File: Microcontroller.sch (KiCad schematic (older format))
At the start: 22 parts, among them J3 Conn_02x03_Counter_Clockwise, U3 STM32F446VET6-sternie, U4 OSCILLATOR-sternie

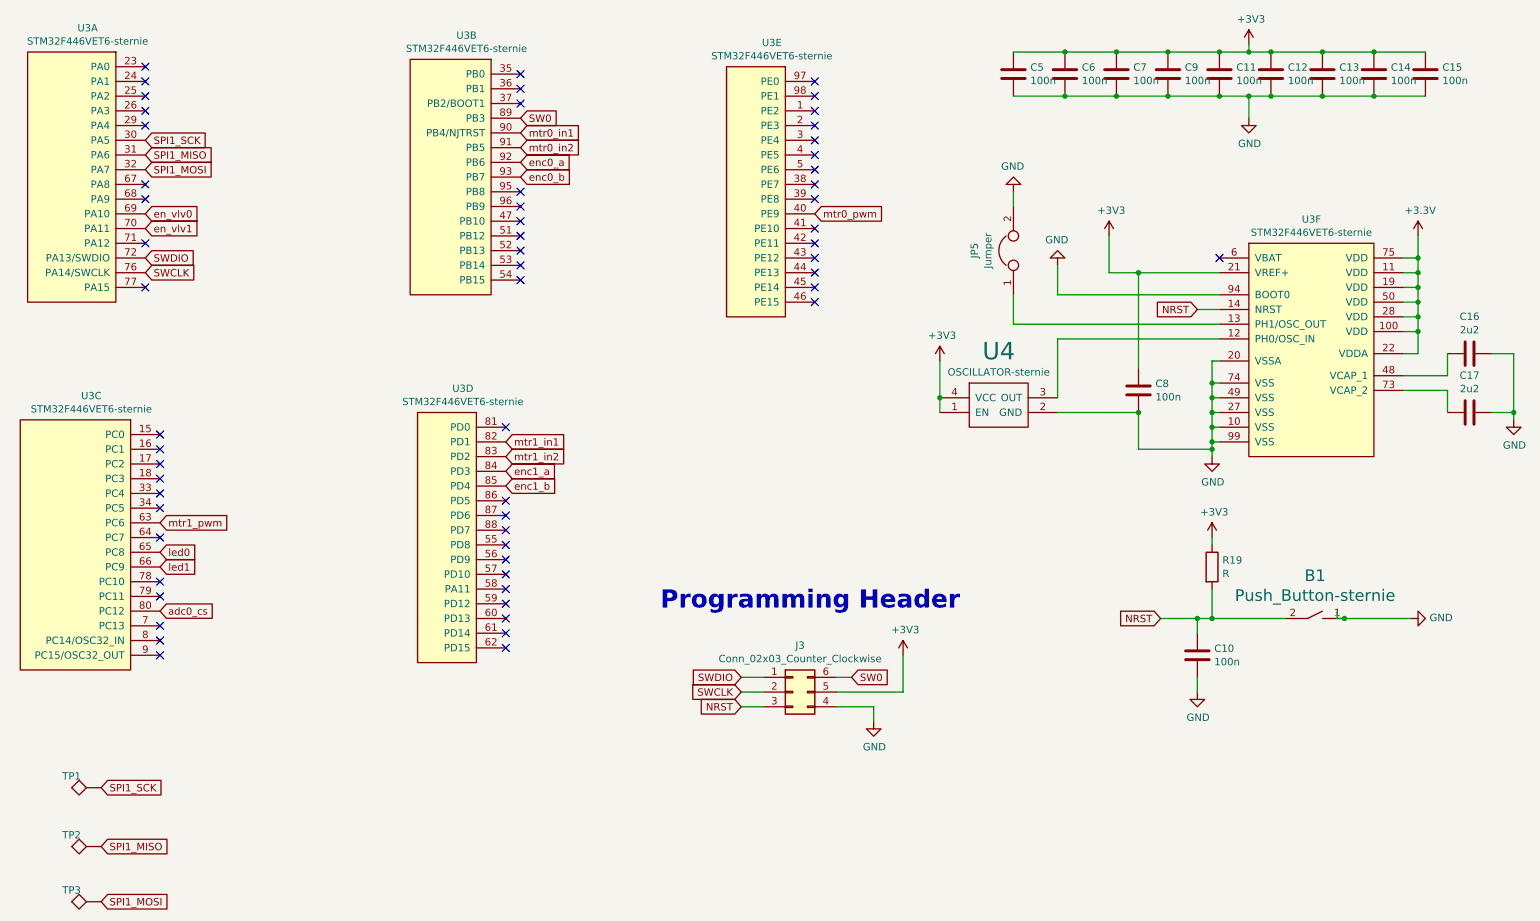
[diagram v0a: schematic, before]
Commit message: Formatting Changes
Made some minor formatting changes. Documented motor channels. Fixed in labels of motor channel.
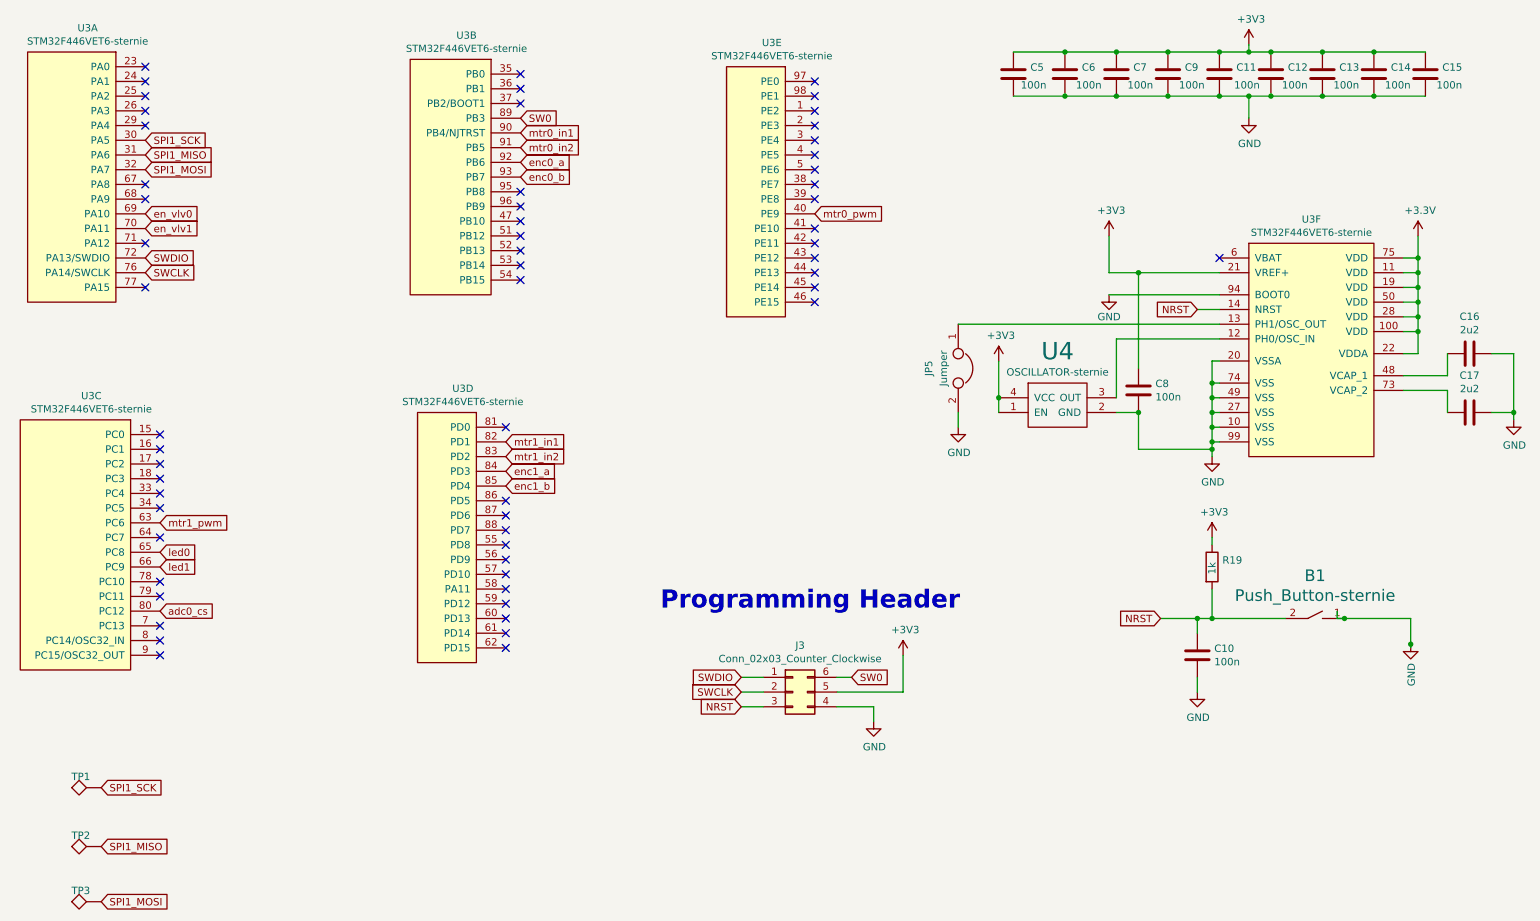
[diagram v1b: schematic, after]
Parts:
- R19: value R -> 1k
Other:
- moved on the sheet: JP5, U4
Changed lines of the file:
@@
 $Descr A4 11693 8268
 encoding utf-8
-Sheet 7 12
+Sheet 4 12
 Title ""
 Date ""
@@
 L bangbang_rev1-rescue:OSCILLATOR-sternie-engine_controller_series3-rescue U4
 U 1 1 5E54009F
-P 7550 3600
-F 0 "U4" H 7550 3966 118 0000 C CNN
-F 1 "OSCILLATOR-sternie" H 7550 3824 50  0000 C CNN
-F 2 "" H 7550 3600 118 0001 C CNN
-F 3 "" H 7550 3600 118 0001 C CNN
-	1    7550 3600
+P 7950 3600
+F 0 "U4" H 7950 3966 118 0000 C CNN
+F 1 "OSCILLATOR-sternie" H 7950 3824 50  0000 C CNN
+F 2 "" H 7950 3600 118 0001 C CNN
+F 3 "" H 7950 3600 118 0001 C CNN
+	1    7950 3600
 	1    0    0    -1
 $EndComp
@@
 	8900 2950 9050 2950
 Wire Wire Line
-	7950 3650 8500 3650
-Connection ~ 8500 3650
-Wire Wire Line
-	7150 3650 7150 3550
-Connection ~ 7150 3550
-Wire Wire Line
-	7150 3550 7150 3300
+	7550 3650 7550 3550
+Connection ~ 7550 3550
+Wire Wire Line
+	7550 3550 7550 3300
 $Comp
 L power:+3V3 #PWR036
 U 1 1 5E5FF2C5
-P 7150 3300
-F 0 "#PWR036" H 7150 3150 50  0001 C CNN
-F 1 "+3V3" H 7165 3473 50  0000 C CNN
-F 2 "" H 7150 3300 50  0001 C CNN
-F 3 "" H 7150 3300 50  0001 C CNN
-	1    7150 3300
-	1    0    0    -1
-$EndComp
-Wire Wire Line
-	7950 2650 7950 2850
-Wire Wire Line
-	7950 2850 9050 2850
+P 7550 3300
+F 0 "#PWR036" H 7550 3150 50  0001 C CNN
+F 1 "+3V3" H 7565 3473 50  0000 C CNN
+F 2 "" H 7550 3300 50  0001 C CNN
+F 3 "" H 7550 3300 50  0001 C CNN
+	1    7550 3300
+	1    0    0    -1
+$EndComp
 $Comp
 L power:+3V3 #PWR039
@@
 $EndComp
 $Comp
-L power:GND #PWR038
-U 1 1 5E604DB8
-P 7950 2650
-F 0 "#PWR038" H 7950 2400 50  0001 C CNN
-F 1 "GND" H 7955 2477 50  0000 C CNN
-F 2 "" H 7950 2650 50  0001 C CNN
-F 3 "" H 7950 2650 50  0001 C CNN
-	1    7950 2650
-	-1   0    0    1
-$EndComp
-Wire Wire Line
-	7950 3550 7950 3150
-Wire Wire Line
-	7950 3150 9050 3150
-Wire Wire Line
-	9050 3050 7650 3050
-Wire Wire Line
-	7650 3050 7650 2850
-$Comp
 L Device:Jumper JP5
 U 1 1 5E60F8B9
-P 7650 2550
-F 0 "JP5" H 7650 2814 50  0000 C CNN
-F 1 "Jumper" H 7650 2723 50  0000 C CNN
-F 2 "" H 7650 2550 50  0001 C CNN
-F 3 "~" H 7650 2550 50  0001 C CNN
-	1    7650 2550
-	0    -1   -1   0
-$EndComp
-Wire Wire Line
-	7650 2250 7650 2150
+P 7275 3350
+F 0 "JP5" H 7275 3150 50  0000 C CNN
+F 1 "Jumper" H 7275 3250 50  0000 C CNN
+F 2 "" H 7275 3350 50  0001 C CNN
+F 3 "~" H 7275 3350 50  0001 C CNN
+	1    7275 3350
+	0    1    1    0
+$EndComp
+Wire Wire Line
+	7275 3650 7275 3750
 $Comp
 L power:GND #PWR037
 U 1 1 5E6156CF
-P 7650 2150
-F 0 "#PWR037" H 7650 1900 50  0001 C CNN
-F 1 "GND" H 7655 1977 50  0000 C CNN
-F 2 "" H 7650 2150 50  0001 C CNN
-F 3 "" H 7650 2150 50  0001 C CNN
-	1    7650 2150
-	-1   0    0    1
+P 7275 3750
+F 0 "#PWR037" H 7275 3500 50  0001 C CNN
+F 1 "GND" H 7280 3577 50  0000 C CNN
+F 2 "" H 7275 3750 50  0001 C CNN
+F 3 "" H 7275 3750 50  0001 C CNN
+	1    7275 3750
+	1    0    0    -1
 $EndComp
 $Comp
@@
 P 8000 1350
 F 0 "C6" H 8115 1396 50  0000 L CNN
-F 1 "100n" H 8115 1305 50  0000 L CNN
+F 1 "100n" H 8075 1275 50  0000 L CNN
 F 2 "" H 8038 1200 50  0001 C CNN
 F 3 "~" H 8000 1350 50  0001 C CNN
@@
 P 8350 1350
 F 0 "C7" H 8465 1396 50  0000 L CNN
-F 1 "100n" H 8465 1305 50  0000 L CNN
+F 1 "100n" H 8425 1275 50  0000 L CNN
 F 2 "" H 8388 1200 50  0001 C CNN
 F 3 "~" H 8350 1350 50  0001 C CNN
@@
 P 8700 1350
 F 0 "C9" H 8815 1396 50  0000 L CNN
-F 1 "100n" H 8815 1305 50  0000 L CNN
+F 1 "100n" H 8775 1275 50  0000 L CNN
 F 2 "" H 8738 1200 50  0001 C CNN
 F 3 "~" H 8700 1350 50  0001 C CNN
@@
 P 9050 1350
 F 0 "C11" H 9165 1396 50  0000 L CNN
-F 1 "100n" H 9165 1305 50  0000 L CNN
+F 1 "100n" H 9150 1275 50  0000 L CNN
 F 2 "" H 9088 1200 50  0001 C CNN
 F 3 "~" H 9050 1350 50  0001 C CNN
@@
 P 9400 1350
 F 0 "C12" H 9515 1396 50  0000 L CNN
-F 1 "100n" H 9515 1305 50  0000 L CNN
+F 1 "100n" H 9475 1275 50  0000 L CNN
 F 2 "" H 9438 1200 50  0001 C CNN
 F 3 "~" H 9400 1350 50  0001 C CNN
@@
 P 9750 1350
 F 0 "C13" H 9865 1396 50  0000 L CNN
-F 1 "100n" H 9865 1305 50  0000 L CNN
+F 1 "100n" H 9825 1275 50  0000 L CNN
 F 2 "" H 9788 1200 50  0001 C CNN
 F 3 "~" H 9750 1350 50  0001 C CNN
@@
 P 10100 1350
 F 0 "C14" H 10215 1396 50  0000 L CNN
-F 1 "100n" H 10215 1305 50  0000 L CNN
+F 1 "100n" H 10175 1275 50  0000 L CNN
 F 2 "" H 10138 1200 50  0001 C CNN
 F 3 "~" H 10100 1350 50  0001 C CNN
@@
 P 10450 1350
 F 0 "C15" H 10565 1396 50  0000 L CNN
-F 1 "100n" H 10565 1305 50  0000 L CNN
+F 1 "100n" H 10525 1275 50  0000 L CNN
 F 2 "" H 10488 1200 50  0001 C CNN
 F 3 "~" H 10450 1350 50  0001 C CNN
@@
 P 7650 1350
 F 0 "C5" H 7765 1396 50  0000 L CNN
-F 1 "100n" H 7765 1305 50  0000 L CNN
+F 1 "100n" H 7700 1275 50  0000 L CNN
 F 2 "" H 7688 1200 50  0001 C CNN
 F 3 "~" H 7650 1350 50  0001 C CNN
@@
 P 9000 4700
 F 0 "R19" H 9070 4746 50  0000 L CNN
-F 1 "R" H 9070 4655 50  0000 L CNN
+F 1 "1k" V 9000 4650 50  0000 L CNN
 F 2 "" V 8930 4700 50  0001 C CNN
 F 3 "~" H 9000 4700 50  0001 C CNN
@@
 L power:GND #PWR045
 U 1 1 5E66819F
-P 10350 5050
-F 0 "#PWR045" H 10350 4800 50  0001 C CNN
-F 1 "GND" V 10355 4922 50  0000 R CNN
-F 2 "" H 10350 5050 50  0001 C CNN
-F 3 "" H 10350 5050 50  0001 C CNN
-	1    10350 5050
-	0    -1   -1   0
+P 10350 5225
+F 0 "#PWR045" H 10350 4975 50  0001 C CNN
+F 1 "GND" V 10355 5097 50  0000 R CNN
+F 2 "" H 10350 5225 50  0001 C CNN
+F 3 "" H 10350 5225 50  0001 C CNN
+	1    10350 5225
+	1    0    0    -1
 $EndComp
 $Comp
@@
 U 1 1 5E750D41
 P 1450 6600
-F 0 "TP2" V 1528 6738 50  0000 L CNN
+F 0 "TP2" V 1525 6675 50  0000 L CNN
 F 1 "TEST" H 1528 6647 50  0001 L CNN
 F 2 "" H 1450 6600 50  0001 C CNN
@@
 U 1 1 5E750D4D
 P 1450 6975
-F 0 "TP3" V 1528 7113 50  0000 L CNN
+F 0 "TP3" V 1525 7050 50  0000 L CNN
 F 1 "TEST" H 1528 7022 50  0001 L CNN
 F 2 "" H 1450 6975 50  0001 C CNN
@@
 U 1 1 5E750D47
 P 1450 6200
-F 0 "TP1" V 1528 6338 50  0000 L CNN
+F 0 "TP1" V 1525 6275 50  0000 L CNN
 F 1 "TEST" H 1528 6247 50  0001 L CNN
 F 2 "" H 1450 6200 50  0001 C CNN
@@
 NoConn ~ 6300 2900
 NoConn ~ 9050 2600
+Wire Wire Line
+	10350 5050 10350 5225
+Connection ~ 10350 5225
+Wire Wire Line
+	10350 5225 10350 5250
+Connection ~ 8500 3650
+Wire Wire Line
+	8350 3650 8500 3650
+Wire Wire Line
+	9050 3150 8350 3150
+Wire Wire Line
+	8350 3150 8350 3550
+Wire Wire Line
+	7275 3050 9050 3050
+$Comp
+L power:GND #PWR038
+U 1 1 5E604DB8
+P 8300 2850
+F 0 "#PWR038" H 8300 2600 50  0001 C CNN
+F 1 "GND" H 8300 2700 50  0000 C CNN
+F 2 "" H 8300 2850 50  0001 C CNN
+F 3 "" H 8300 2850 50  0001 C CNN
+	1    8300 2850
+	1    0    0    -1
+$EndComp
+Wire Wire Line
+	8300 2850 9050 2850
 $EndSCHEMATC

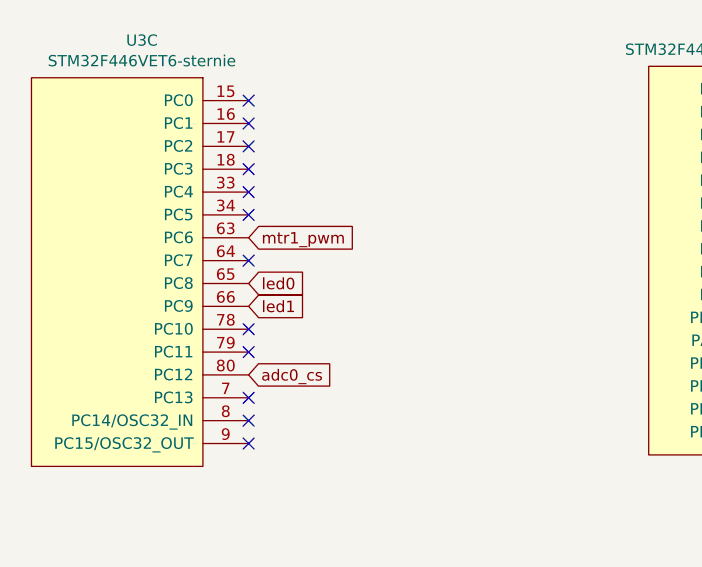
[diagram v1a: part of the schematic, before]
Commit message: renamed motor controller input name and moved adc pinouts
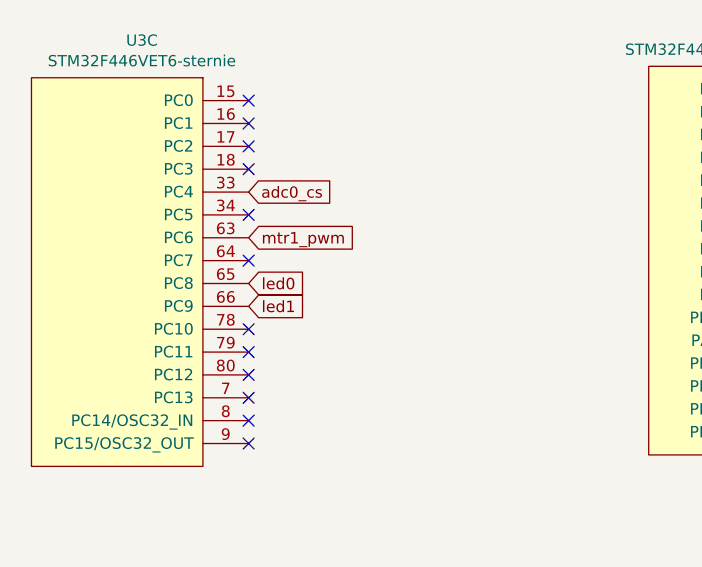
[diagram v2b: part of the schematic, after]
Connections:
- net adc0_cs: now also U3.33 (PC4); no longer U3.80 (PC12)
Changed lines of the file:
@@
 Text GLabel 4300 1650 2    50   Input ~ 0
 SW0
-Text GLabel 1850 5000 2    49   Input ~ 0
+Text GLabel 1850 4200 2    49   Input ~ 0
 adc0_cs
 NoConn ~ 1750 1300
@@
 NoConn ~ 1850 4000
 NoConn ~ 1850 4100
-NoConn ~ 1850 4200
 NoConn ~ 1850 4300
 NoConn ~ 1850 4500
@@
 Wire Wire Line
 	8300 2850 9050 2850
+NoConn ~ 1850 5000
 $EndSCHEMATC
